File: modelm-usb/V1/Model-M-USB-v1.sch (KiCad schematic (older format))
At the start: 60 parts, among them J1 Conn_01x16, J2 Conn_01x08, J3 Conn_01x05_Male, J4 USB_B, J5 Conn_01x02_Male, J6 Conn_01x04, J7 Conn_01x05_Male, J8 Conn_01x02, J9 AVR-ISP-6, Q1 2N7002, SW1 SW_Push, U1 ATmega32U4-MU, U2 PRTR5V0U2X, U3 74HC165, U4 MAX809T, U5 74HC165, Y1 16.0MHz, Y2 16.0MHz

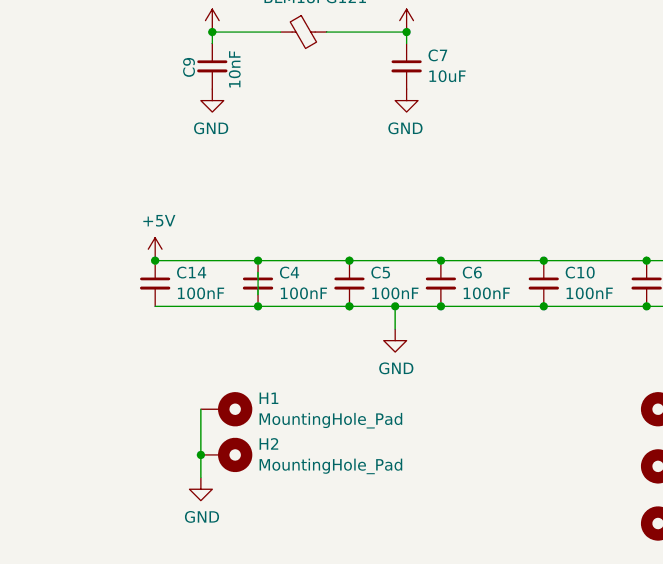
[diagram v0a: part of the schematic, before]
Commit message: Component Identifiers and BOM/Placement for jlcpcb
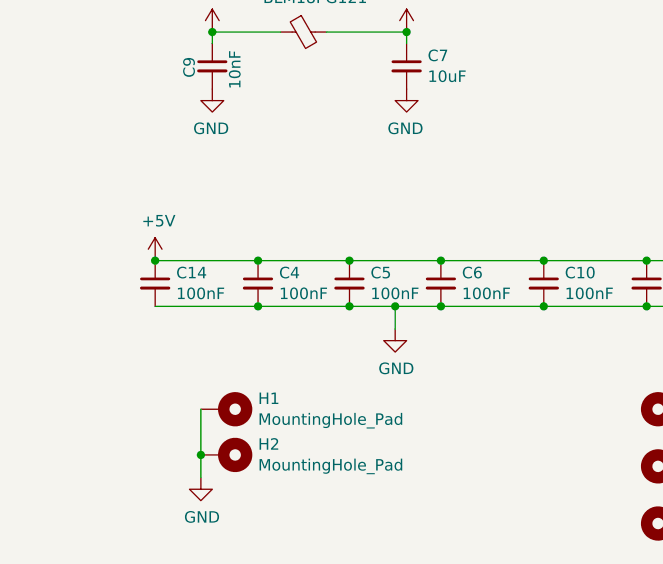
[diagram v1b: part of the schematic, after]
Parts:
- C1, C2: LCSC (none) -> C1656
- C10, C11, C12, C13, C14, C4, C5, C6, C8: LCSC (none) -> C14663
- C3: LCSC (none) -> C15849
- C7: LCSC (none) -> C19702
- C9: LCSC (none) -> C57112
- D1: LCSC (none) -> C72038
- FB1: LCSC (none) -> C73100
- Q1: LCSC (none) -> C8545
- R1, R14, R17, R22, R5, R6: LCSC (none) -> C25804
- R10, R11, R8, R9: LCSC (none) -> C12027
- R12, R2: LCSC (none) -> C21190
- R13, R18, R19, R20: LCSC (none) -> C21189
- R15, R16: LCSC (none) -> C17958
- R3, R4: LCSC (none) -> C23345
- U1: LCSC (none) -> C44854
- U2: LCSC (none) -> C316030
- U3, U5: LCSC (none) -> C5613
- U4: LCSC (none) -> C16711
- Y1: LCSC (none) -> C12676
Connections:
- wire segments 195 -> 194

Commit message: add R-C-compensation board
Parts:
- J4: symbol Connector:USB_B -> Model-M-USB-v1-rescue:USB_B-Connector
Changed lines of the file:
@@
 $EndComp
 $Comp
-L Connector:USB_B J4
+L Model-M-USB-v1-rescue:USB_B-Connector J4
 U 1 1 5EC21E0A
 P 1050 3400
